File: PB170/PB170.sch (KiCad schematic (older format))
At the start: 33 parts, among them J1 USB_C_Receptacle_USB2.0-Conne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, J2 USB_B_Micro, Q1 P-MOSFET-MLP_HS, Q2 BC817, SW1 SW_MEC_5E, SW2 SW_MEC_5E

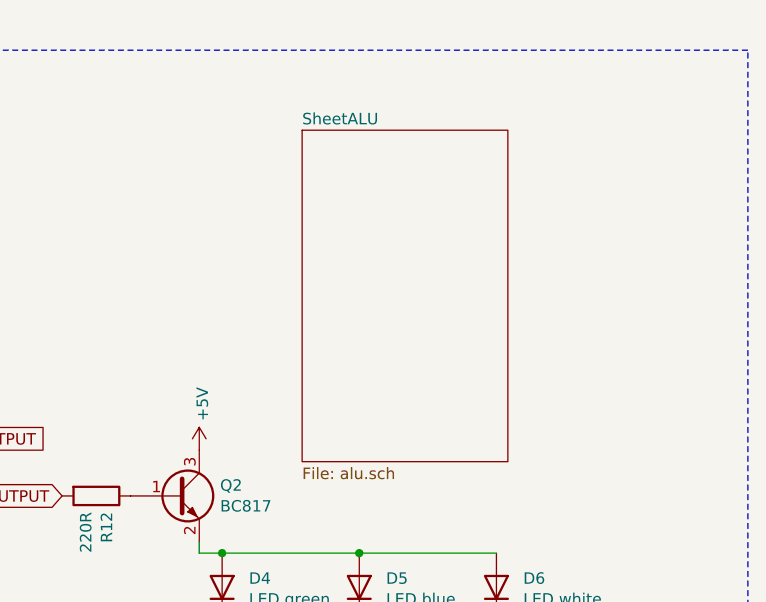
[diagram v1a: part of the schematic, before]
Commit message: Add alu output flags
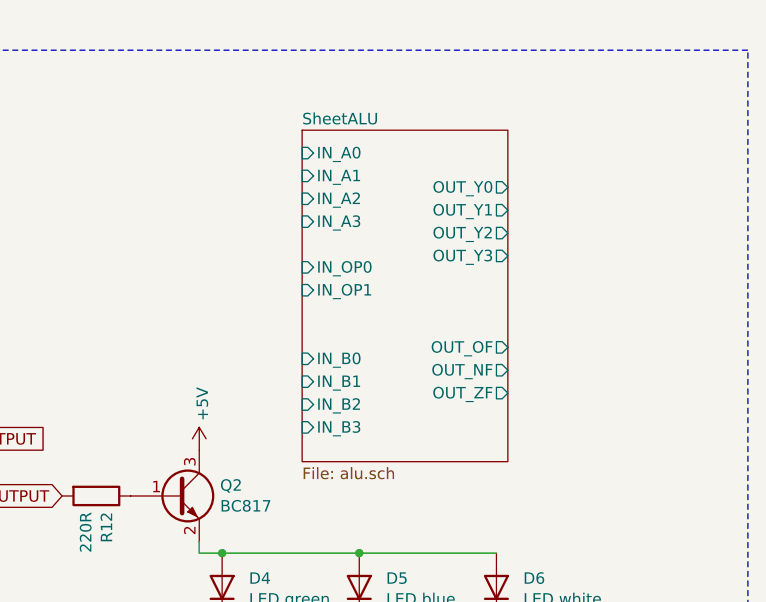
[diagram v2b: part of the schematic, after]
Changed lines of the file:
@@
 F0 "SheetALU" 50
 F1 "alu.sch" 50
+F2 "IN_A0" I L 8750 1400 50
+F3 "IN_B0" I L 8750 2300 50
+F4 "IN_A1" I L 8750 1500 50
+F5 "IN_A2" I L 8750 1600 50
+F6 "IN_A3" I L 8750 1700 50
+F7 "IN_B1" I L 8750 2400 50
+F8 "IN_B2" I L 8750 2500 50
+F9 "IN_B3" I L 8750 2600 50
+F10 "IN_OP0" I L 8750 1900 50
+F11 "IN_OP1" I L 8750 2000 50
+F12 "OUT_Y0" O R 9650 1550 50
+F13 "OUT_Y1" O R 9650 1650 50
+F14 "OUT_Y2" O R 9650 1750 50
+F15 "OUT_Y3" O R 9650 1850 50
+F16 "OUT_OF" O R 9650 2250 50
+F17 "OUT_NF" O R 9650 2350 50
+F18 "OUT_ZF" O R 9650 2450 50
 $EndSheet
 $EndSCHEMATC

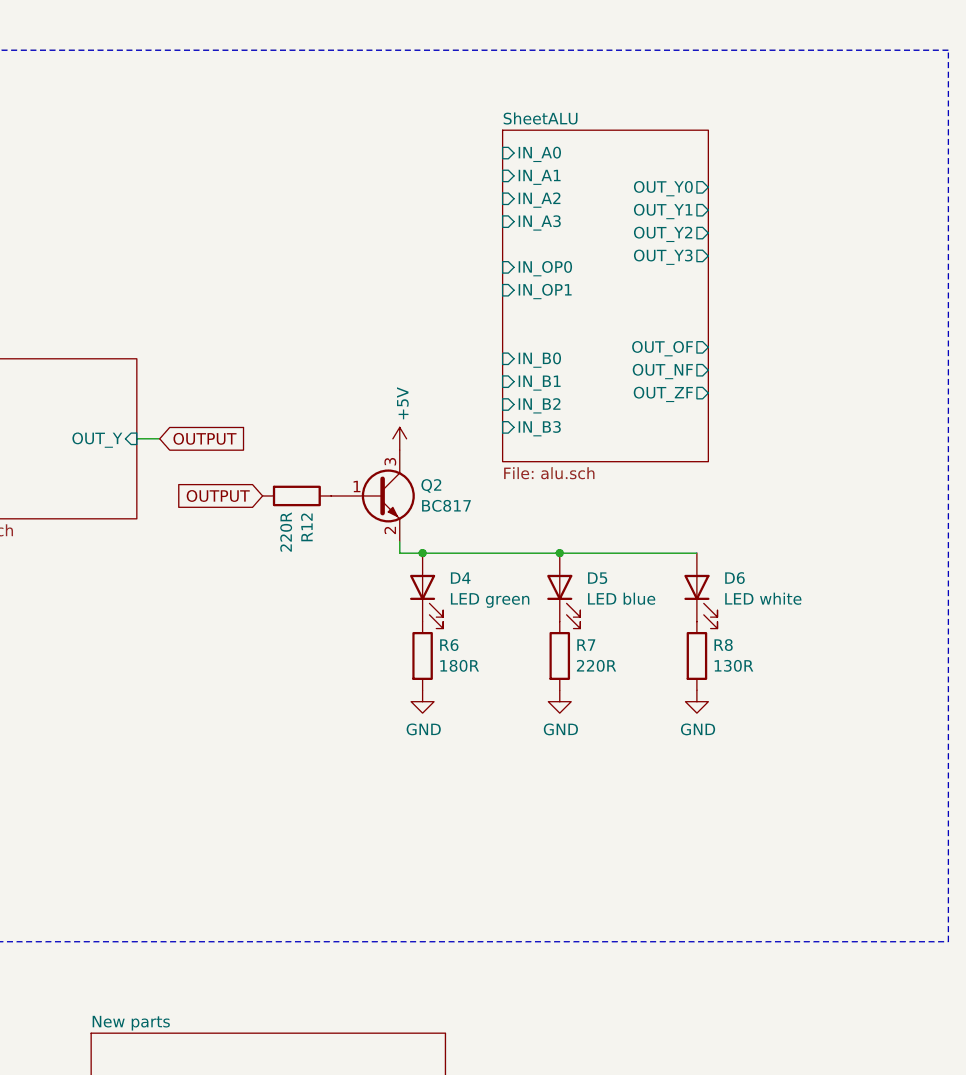
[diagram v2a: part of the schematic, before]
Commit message: Create empty InputSheet and OutputSheet
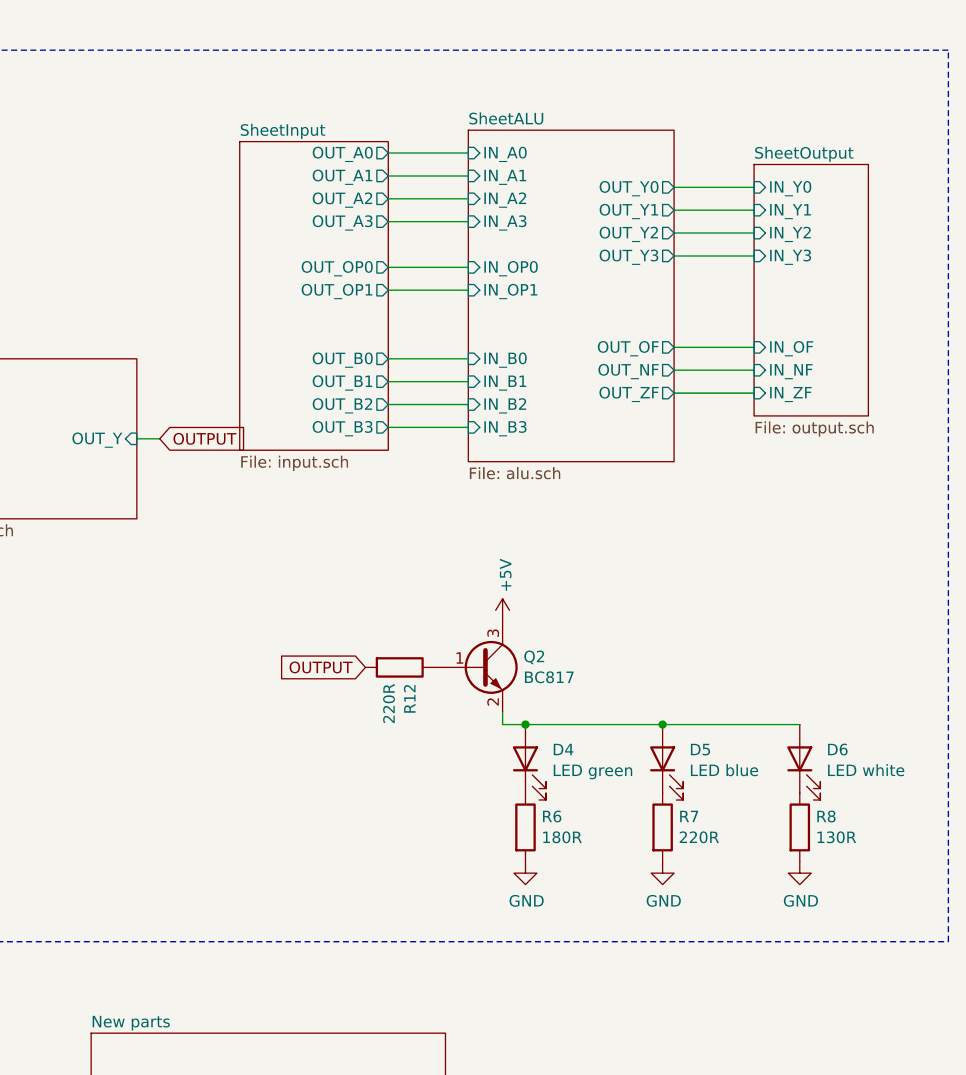
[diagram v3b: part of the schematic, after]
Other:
- moved on the sheet: D4, D5, D6, Q2, R12, R6, R7, R8

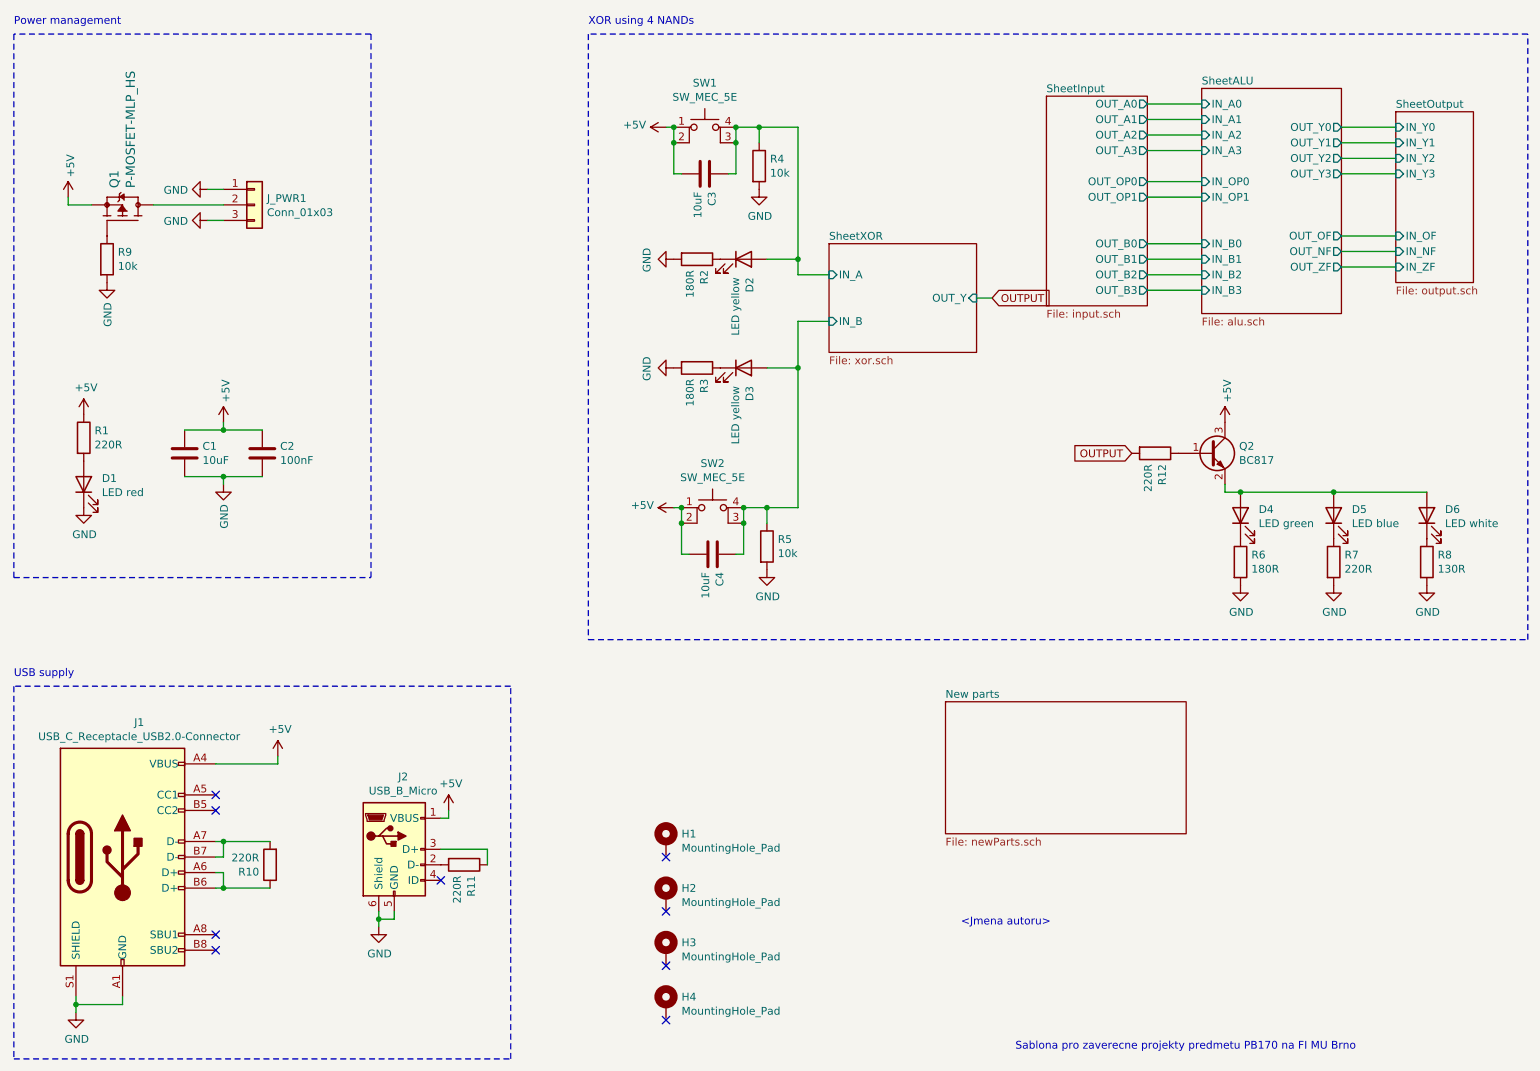
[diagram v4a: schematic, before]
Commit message: Remove xor from the main sheet
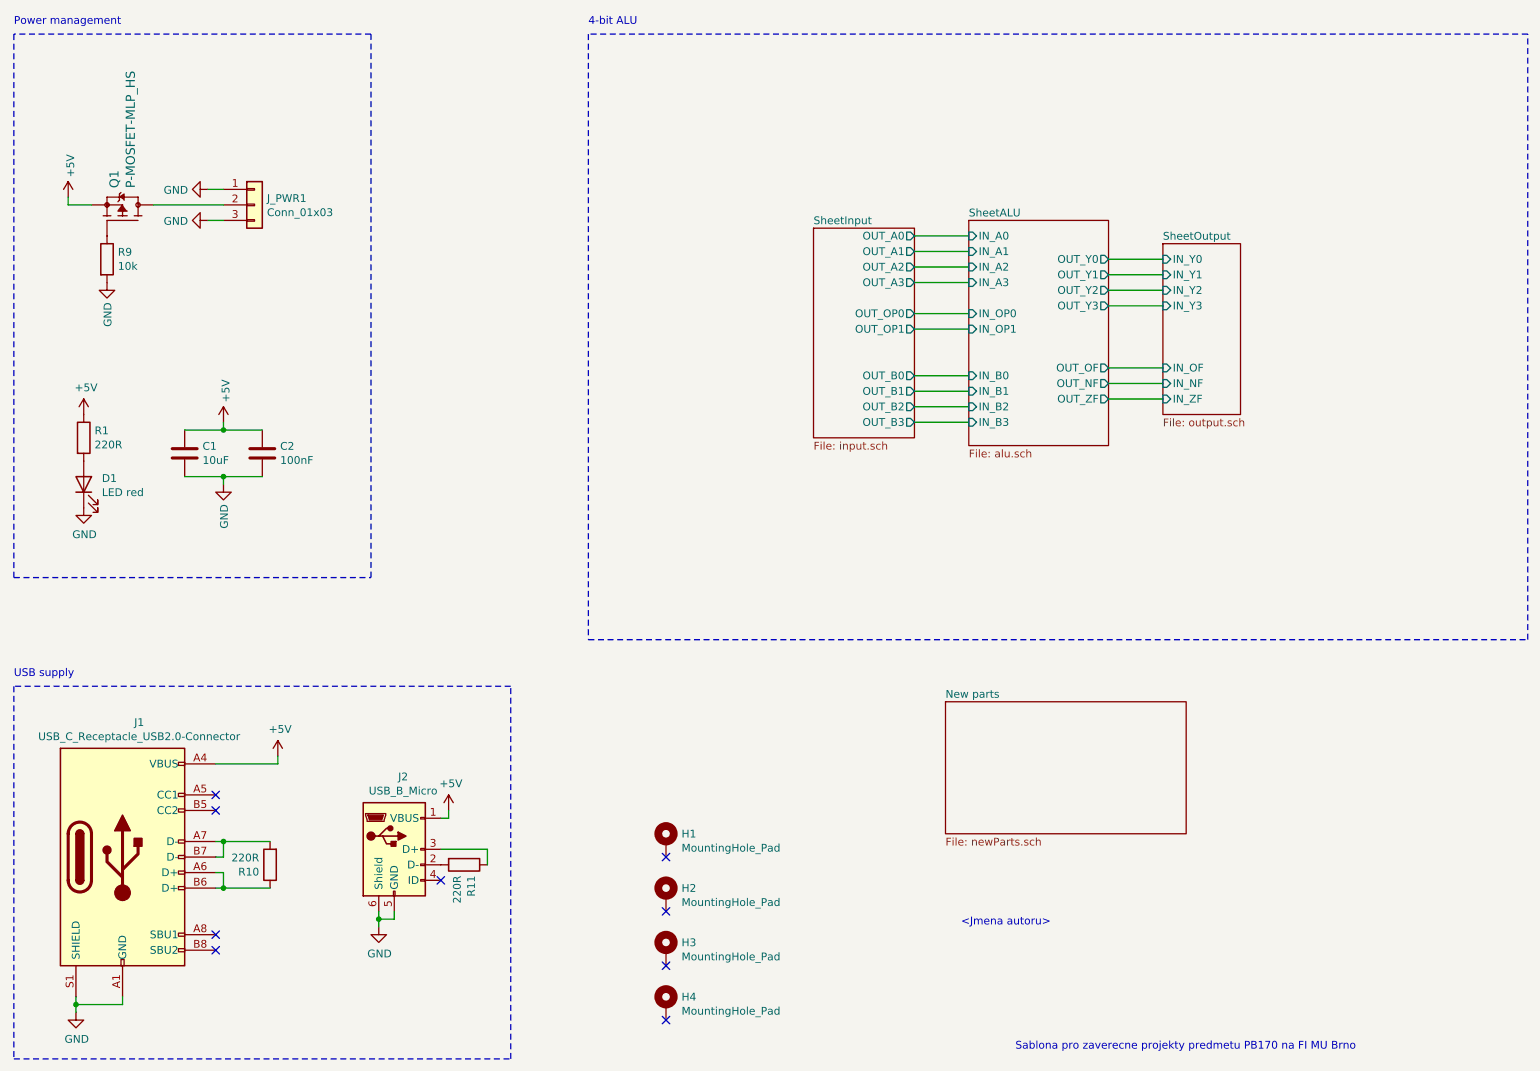
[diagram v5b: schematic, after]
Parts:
- removed C3, C4: 10uF, Capacitors_SMD:C_0805, symbol Device:C
- removed D2, D3: LED yellow, LEDs:LED_0603, symbol Device:LED
- removed D4: LED green, LEDs:LED_0603, symbol Device:LED
- removed D5: LED blue, LEDs:LED_0603, symbol Device:LED
- removed D6: LED white, LEDs:LED_0603, symbol Device:LED
- removed Q2: BC817, TO_SOT_Packages_SMD:SOT-23, symbol Transistor_BJT:BC817
- removed R12, R7: 220R, Resistors_SMD:R_0603, symbol Device:R
- removed R2, R3, R6: 180R, Resistors_SMD:R_0603, symbol Device:R
- removed R4, R5: 10k, Resistors_SMD:R_0603, symbol Device:R
- removed R8: 130R, Resistors_SMD:R_0603, symbol Device:R
- removed SW1, SW2: SW_MEC_5E, PB170:TactileSwitch_C381064, symbol Switch:SW_MEC_5E
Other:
- note added: "4-bit ALU"
- note removed: "XOR using 4 NANDs"
